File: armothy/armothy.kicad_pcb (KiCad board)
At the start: 2 copper layers, 90.2 x 59.7 mm, 21 parts, among them J1 I2C, J2 UART, J3 motZ, J4 pump, J5 valve, J6 Encoder, J7 Limit switch, J8 12V_PWR, J9 Conn_01x03_Female, U1 L293D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

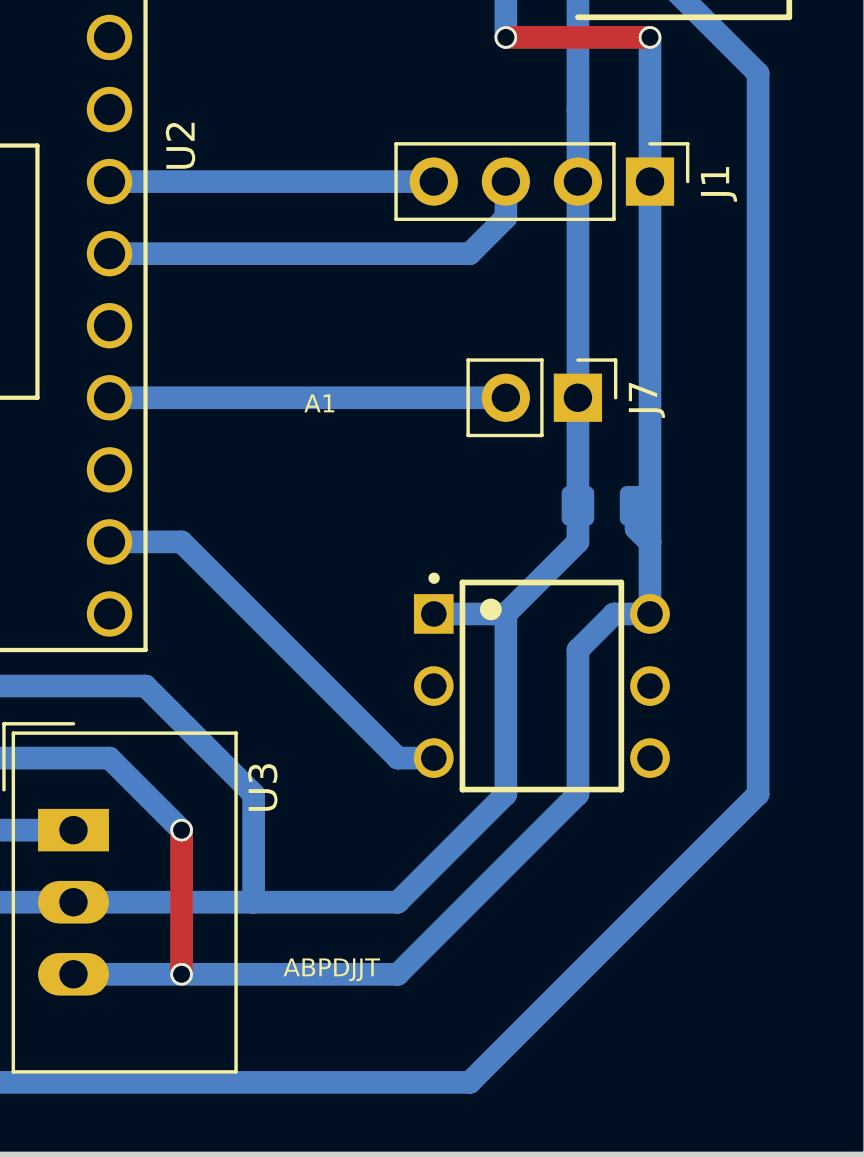
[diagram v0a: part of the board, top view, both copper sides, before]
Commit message: Adds 3D models, fix ABPDJJT footprint (fix #1).
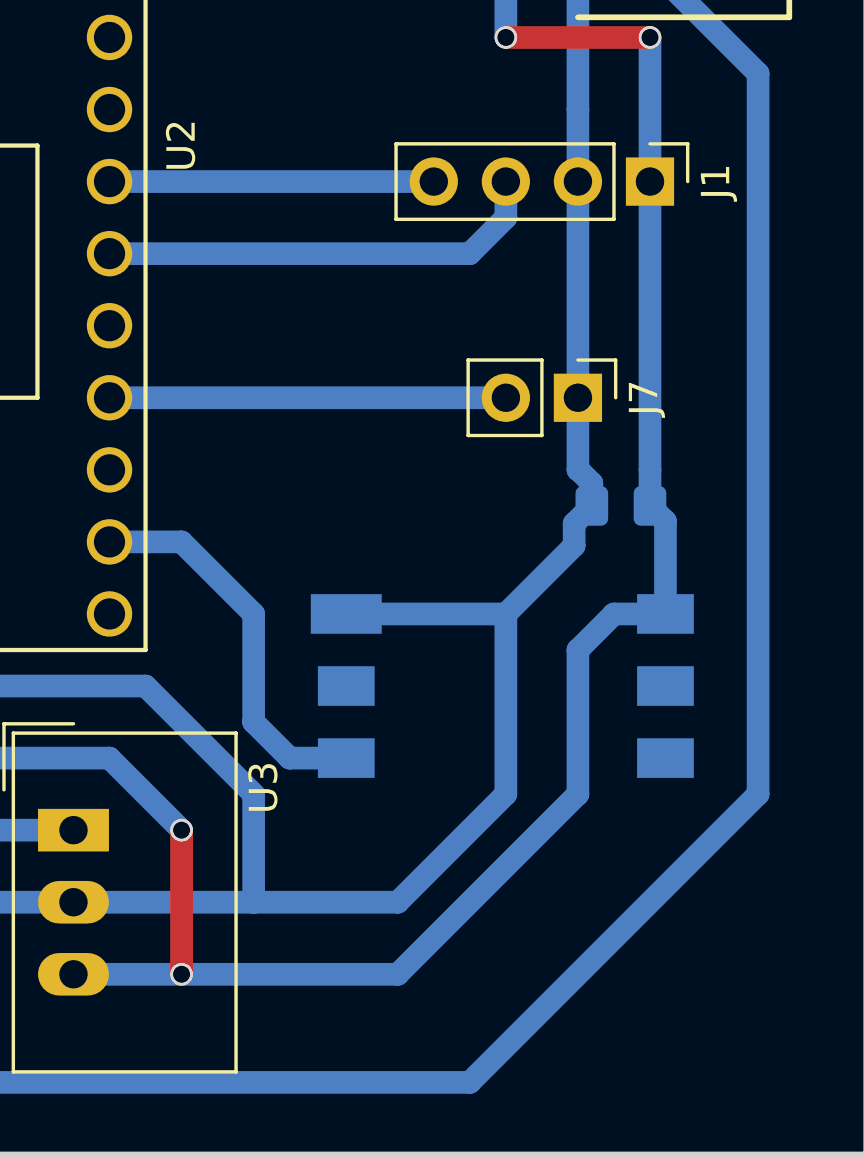
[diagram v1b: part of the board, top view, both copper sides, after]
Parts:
- A1: moved to B.Cu
- D1: footprint LED_SMD:LED_WS2812B_PLCC4_5.0x5.0mm_P3.2mm -> leds:LED_WS2812B_5.0x5.0mm
- moved A1 1.27 mm to (156.2, 101.6)
- moved C1 0.49 mm to (160.3, 95.2)
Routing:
- net GND: track 320.0 -> 323.5 mm
- net /PRESSURE: track 14.6 -> 13.7 mm
- net +5V: track 203.7 -> 203.0 mm

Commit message: Armothy controller V2.0
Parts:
- removed U1: L293D, Package_DIP:DIP-16_W7.62mm_LongPads
- added C6: 100n, Capacitor_SMD:C_0805_2012Metric_Pad1.15x1.40mm_HandSolder, B.Cu at (138.4, 103.9)
- added C7: 100n, Capacitor_SMD:C_0805_2012Metric_Pad1.15x1.40mm_HandSolder, B.Cu at (135.9, 103.9)
- added C8: 100n, Capacitor_SMD:C_0805_2012Metric_Pad1.15x1.40mm_HandSolder, B.Cu at (123.2, 100.3)
- added J10: I2C, Connector_PinHeader_2.54mm:PinHeader_1x04_P2.54mm_Vertical, F.Cu at (154.9, 77.5)
- added Q1: IRL6283M, mosfets:SOT-23, B.Cu at (122.1, 81.6)
- added Q2: IRL6283M, mosfets:SOT-23, B.Cu at (122.1, 86.0)
- added R3: 2.2K, Resistor_SMD:R_0805_2012Metric_Pad1.15x1.40mm_HandSolder, B.Cu at (138.0, 83.8)
- added R4: 2.2K, Resistor_SMD:R_0805_2012Metric_Pad1.15x1.40mm_HandSolder, B.Cu at (138.0, 86.4)
- added R5: 5K, Resistor_SMD:R_0805_2012Metric_Pad1.15x1.40mm_HandSolder, B.Cu at (130.8, 95.0)
- added R6: 10K, Resistor_SMD:R_0805_2012Metric_Pad1.15x1.40mm_HandSolder, B.Cu at (133.3, 95.0)
- added R7: 100, Resistor_SMD:R_0805_2012Metric_Pad1.15x1.40mm_HandSolder, B.Cu at (139.2, 99.3)
- added REF**: MountingHole_3.2mm_M3_Pad, MountingHole:MountingHole_3.2mm_M3_Pad, F.Cu at (157.0, 60.0)
- added REF**: MountingHole_3.2mm_M3_Pad, MountingHole:MountingHole_3.2mm_M3_Pad, F.Cu at (107.0, 120.0)
- added REF**: MountingHole_3.2mm_M3_Pad, MountingHole:MountingHole_3.2mm_M3_Pad, F.Cu at (107.0, 60.0)
- added REF**: MountingHole_3.2mm_M3_Pad, MountingHole:MountingHole_3.2mm_M3_Pad, F.Cu at (157.0, 120.0)
- added TP1: TestPoint, TestPoint:TestPoint_Pad_D1.0mm, B.Cu at (138.4, 71.1)
- added TP2: TestPoint, TestPoint:TestPoint_Pad_D1.0mm, B.Cu at (138.4, 73.7)
- added TP3: TestPoint, TestPoint:TestPoint_Pad_D1.0mm, B.Cu at (138.4, 78.7)
- added TP4: TestPoint, TestPoint:TestPoint_Pad_D1.0mm, B.Cu at (138.4, 76.2)
- added U5: ACS712xLCTR-05B, Package_SO:SOIC-8_3.9x4.9mm_P1.27mm, B.Cu at (129.5, 105.4)
- added U6: A4953_LJ, Package_SO:SOIC-8-1EP_3.9x4.9mm_P1.27mm_EP2.35x2.35mm, B.Cu at (119.4, 99.1)
- A1, C1: moved to F.Cu
- D1: value WS2812B -> LED; footprint leds:LED_WS2812B_5.0x5.0mm -> LED_SMD:LED_0805_2012Metric_Pad1.15x1.40mm_HandSolder
- moved C5 46.2 mm to (153.9, 88.3)
- moved J9 46.2 mm to (115.6, 91.4)
- moved R1 38.2 mm to (130.2, 88.5), turned to 90 degrees
- moved D1 31.0 mm to (135.9, 99.3), turned to 90 degrees
- moved J6 25.9 mm to (114.3, 73.7)
- moved J5 25.0 mm to (114.3, 81.3)
- moved J3 24.5 mm to (116.8, 108.0), turned to 270 degrees
- moved C3 18.1 mm to (118.1, 115.3), turned to 90 degrees
- moved C2 17.8 mm to (131.4, 116.8), turned to 90 degrees
- moved C1 17.1 mm to (145.4, 103.8), turned to 90 degrees
- moved J4 16.2 mm to (114.3, 86.4), turned to 90 degrees
- moved C4 13.3 mm to (121.3, 112.8), turned to 270 degrees
- moved J8 12.5 mm to (113.0, 114.3), turned to 0 degrees
- moved U4 10.9 mm to (124.5, 116.8), turned to 90 degrees
- moved U3 10.2 mm to (142.2, 116.8), turned to 90 degrees
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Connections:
- A1 pad 2: Net-(A1-Pad2) -> (no net)
- A1 pad 4: Net-(A1-Pad4) -> (no net)
- A1 pad 5: Net-(A1-Pad5) -> (no net)
- C2 pad 1: /POWER -> +12V
- C3 pad 1: /POWER -> +12V
- C5 pad 1: +5V -> /LIM_SWITCH
- D1 pad 1: +5V -> GND
- J4 pad 1: /POWER -> +12V
- J5 pad 1: Net-(J5-Pad1) -> +12V
- J5 pad 2: GND -> Net-(J5-Pad2)
- J8 pad 2: /POWER -> +12V
- U2 pad 12: /MOTORZ_PWM -> /MOTORZ_A
- U2 pad 13: /ENC_A -> (no net)
- U2 pad 14: /ENC_B -> (no net)
- U2 pad 20: Net-(U2-Pad20) -> /STATUS_LED
- U2 pad 22: Net-(U2-Pad22) -> /Z_CURRENT
- U2 pad 24: Net-(U2-Pad24) -> (no net)
- U2 pad 27: Net-(U2-Pad27) -> (no net)
- U2 pad 4: /MOTORZ_A -> /ENC_B
- U2 pad 5: Net-(U2-Pad5) -> /ENC_A
- U2 pad 6: /RGB_LED -> (no net)
- U3 pad 1: /POWER -> +12V
- U4 pad 1: /POWER -> +12V
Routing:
- net GND: track 323.5 -> 224.5 mm, vias 0 -> 5
- net +12V: track 0.00 -> 87.7 mm, vias 0 -> 2
- net /POWER: track 77.8 -> 0.00 mm, vias 2 -> 0
- net /RX_DYN: track 63.6 -> 6.18 mm, vias 2 -> 0
- net /VALVE_CTRL: track 60.1 -> 4.07 mm
- net /MOTORZ_PWM: track 45.3 -> 0.00 mm, vias 2 -> 0
- net /MOTORZ_A: track 52.8 -> 8.62 mm, vias 2 -> 0
- net +10V: track 77.0 -> 39.6 mm
- net /PUMP_CTRL: track 28.2 -> 4.34 mm
- net /MOTORZ_B: track 28.2 -> 10.9 mm
- net +5V: track 203.0 -> 189.0 mm, vias 8 -> 3
- net Net-(R5-Pad1): track 0.00 -> 12.0 mm
- net Net-(U5-Pad3): track 0.00 -> 11.7 mm
- net /Z_CURRENT: track 0.00 -> 11.4 mm
- net /RGB_LED: track 10.3 -> 0.00 mm
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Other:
- board size 90.2 x 59.7 mm -> 58 x 68 mm
- net class Default: via_dia 0.8 -> 1; via_drill 0.6 -> 0.8
- board text added: "Armothy v2"
- board text added: "Dyn"
- board text added: "ENC"
- board text added: "Fab@RustyDucks 2019"
- board text added: "I2C"
- board text added: "Limit"
- board text added: "Pump"
- board text added: "U1"
- board text added: "USB"
- board text added: "Valve"
- board text added: "Z"

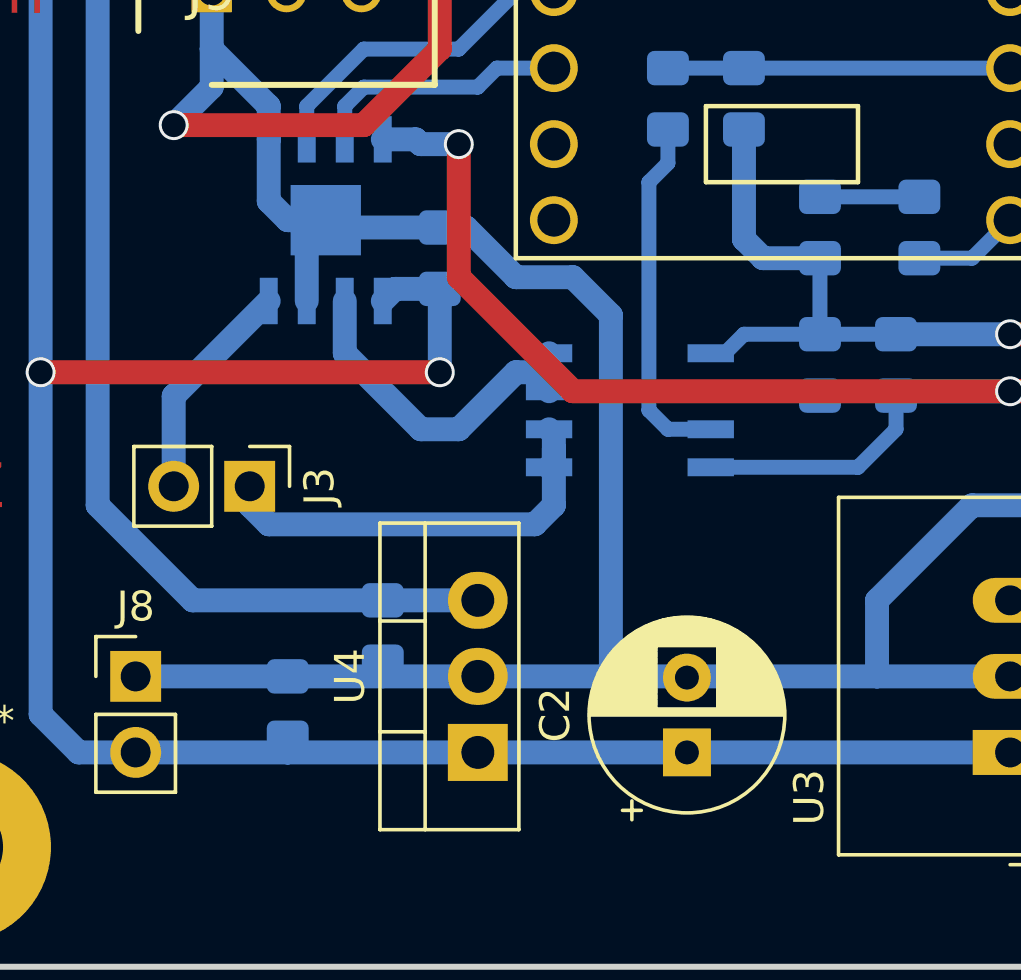
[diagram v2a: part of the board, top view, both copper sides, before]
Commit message: Changes LED footprint.
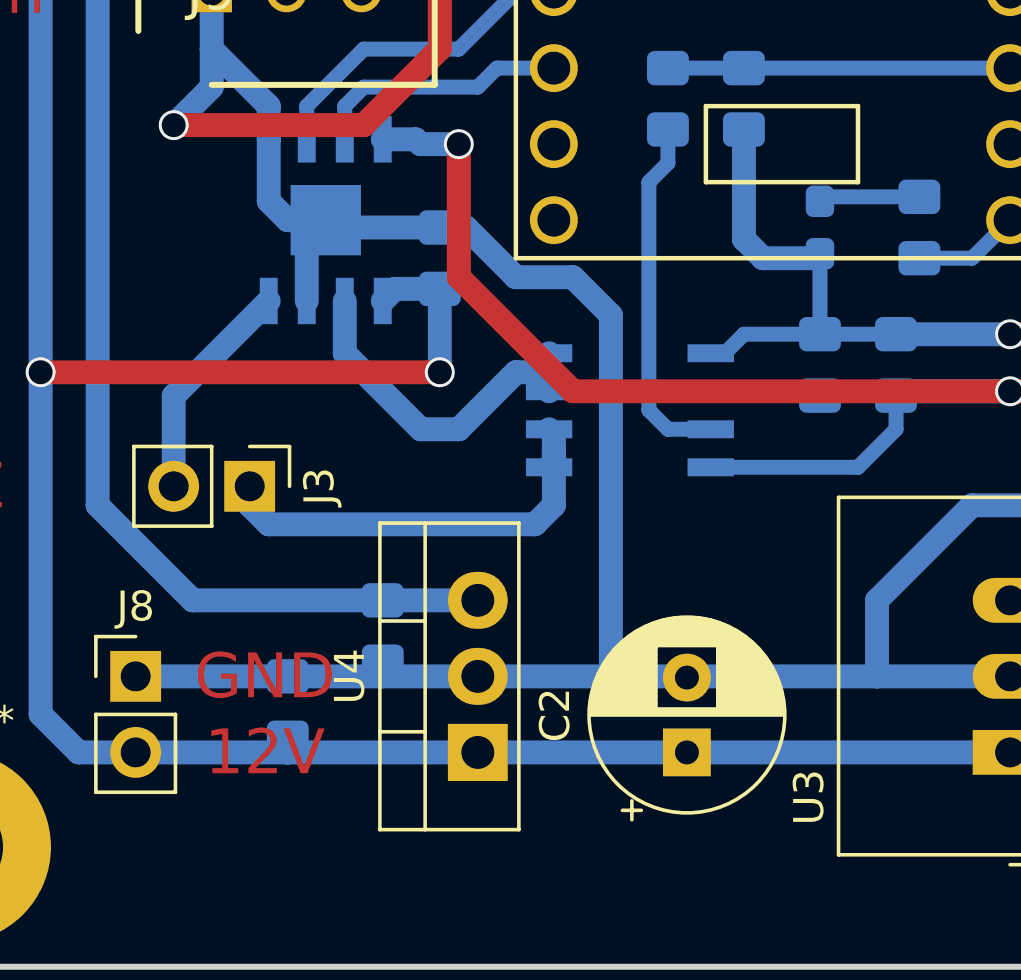
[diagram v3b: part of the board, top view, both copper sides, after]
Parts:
- D1: footprint LED_SMD:LED_0805_2012Metric_Pad1.15x1.40mm_HandSolder -> LED_SMD:LED_0603_1608Metric_Pad1.05x0.95mm_HandSolder
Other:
- board text added: "12V"
- board text added: "GND"
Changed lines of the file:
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@@
   (general
     (thickness 1.6)
-    (drawings 15)
+    (drawings 17)
     (tracks 231)
     (zones 0)
@@
   )
   (page A4)
+  (title_block
+    (title "Armothy controller")
+    (date 2019-02-18)
+    (rev 2.0)
+    (comment 1 Fabien-B)
+  )
   (layers
     (0 F.Cu signal)
@@
   )
   (setup
-    (last_trace_width 0.8)
+    (last_trace_width 0.508)
     (user_trace_width 0.3)
     (user_trace_width 0.5)
@@
     )
   )
-  (module LED_SMD:LED_0805_2012Metric_Pad1.15x1.40mm_HandSolder (layer B.Cu)
-    (at 135.89 99.305 90)
-    (descr "LED SMD 0805 (2012 Metric), square (rectangular) end terminal, IPC_7351 nominal, (Body size source: https://docs.google.com/spreadsheets/d/1BsfQQcO9C6DZCsRaXUlFlo91Tg2WpOkGARC1WS5S8t0/edit?usp=sharing), generated with kicad-footprint-generator")
-    (tags "LED handsolder")
-    (attr smd)
-    (fp_text reference D1 (at 0 1.65 90) (layer B.SilkS)
-      (effects (font (size 1 1) (thickness 0.15)) (justify mirror))
-    )
-    (fp_text value LED (at 0 -1.65 90) (layer B.Fab)
-      (effects (font (size 1 1) (thickness 0.15)) (justify mirror))
-    )
-    (fp_line (start 1 0.6) (end -0.7 0.6) (layer B.Fab) (width 0.1))
-    (fp_line (start -0.7 0.6) (end -1 0.3) (layer B.Fab) (width 0.1))
-    (fp_line (start -1 0.3) (end -1 -0.6) (layer B.Fab) (width 0.1))
-    (fp_line (start -1 -0.6) (end 1 -0.6) (layer B.Fab) (width 0.1))
-    (fp_line (start 1 -0.6) (end 1 0.6) (layer B.Fab) (width 0.1))
-    (fp_line (start 1 0.96) (end -1.86 0.96) (layer B.SilkS) (width 0.12))
-    (fp_line (start -1.86 0.96) (end -1.86 -0.96) (layer B.SilkS) (width 0.12))
-    (fp_line (start -1.86 -0.96) (end 1 -0.96) (layer B.SilkS) (width 0.12))
-    (fp_line (start -1.85 -0.95) (end -1.85 0.95) (layer B.CrtYd) (width 0.05))
-    (fp_line (start -1.85 0.95) (end 1.85 0.95) (layer B.CrtYd) (width 0.05))
-    (fp_line (start 1.85 0.95) (end 1.85 -0.95) (layer B.CrtYd) (width 0.05))
-    (fp_line (start 1.85 -0.95) (end -1.85 -0.95) (layer B.CrtYd) (width 0.05))
-    (fp_text user %R (at 0 0 90) (layer B.Fab)
-      (effects (font (size 0.5 0.5) (thickness 0.08)) (justify mirror))
-    )
-    (pad 1 smd roundrect (at -1.025 0 90) (size 1.15 1.4) (layers B.Cu B.Paste B.Mask) (roundrect_rratio 0.217391)
-      (net 1 GND))
-    (pad 2 smd roundrect (at 1.025 0 90) (size 1.15 1.4) (layers B.Cu B.Paste B.Mask) (roundrect_rratio 0.217391)
-      (net 15 "Net-(D1-Pad2)"))
-    (model ${KISYS3DMOD}/LED_SMD.3dshapes/LED_0805_2012Metric.wrl
-      (at (xyz 0 0 0))
-      (scale (xyz 1 1 1))
-      (rotate (xyz 0 0 0))
-    )
-  )
   (module Connector_PinHeader_2.54mm:PinHeader_1x04_P2.54mm_Vertical (layer F.Cu)
     (at 154.94 77.47 270)
@@
       (net 32 "Net-(TP4-Pad1)"))
   )
+  (module LED_SMD:LED_0603_1608Metric_Pad1.05x0.95mm_HandSolder (layer B.Cu)
+    (at 135.89 99.305 90)
+    (descr "LED SMD 0603 (1608 Metric), square (rectangular) end terminal, IPC_7351 nominal, (Body size source: http://www.tortai-tech.com/upload/download/2011102023233369053.pdf), generated with kicad-footprint-generator")
+    (tags "LED handsolder")
+    (attr smd)
+    (fp_text reference D1 (at 0 1.43 90) (layer B.SilkS)
+      (effects (font (size 1 1) (thickness 0.15)) (justify mirror))
+    )
+    (fp_text value LED (at 0 -1.43 90) (layer B.Fab)
+      (effects (font (size 1 1) (thickness 0.15)) (justify mirror))
+    )
+    (fp_line (start 0.8 0.4) (end -0.5 0.4) (layer B.Fab) (width 0.1))
+    (fp_line (start -0.5 0.4) (end -0.8 0.1) (layer B.Fab) (width 0.1))
+    (fp_line (start -0.8 0.1) (end -0.8 -0.4) (layer B.Fab) (width 0.1))
+    (fp_line (start -0.8 -0.4) (end 0.8 -0.4) (layer B.Fab) (width 0.1))
+    (fp_line (start 0.8 -0.4) (end 0.8 0.4) (layer B.Fab) (width 0.1))
+    (fp_line (start 0.8 0.735) (end -1.66 0.735) (layer B.SilkS) (width 0.12))
+    (fp_line (start -1.66 0.735) (end -1.66 -0.735) (layer B.SilkS) (width 0.12))
+    (fp_line (start -1.66 -0.735) (end 0.8 -0.735) (layer B.SilkS) (width 0.12))
+    (fp_line (start -1.65 -0.73) (end -1.65 0.73) (layer B.CrtYd) (width 0.05))
+    (fp_line (start -1.65 0.73) (end 1.65 0.73) (layer B.CrtYd) (width 0.05))
+    (fp_line (start 1.65 0.73) (end 1.65 -0.73) (layer B.CrtYd) (width 0.05))
+    (fp_line (start 1.65 -0.73) (end -1.65 -0.73) (layer B.CrtYd) (width 0.05))
+    (fp_text user %R (at 0 0 90) (layer B.Fab)
+      (effects (font (size 0.4 0.4) (thickness 0.06)) (justify mirror))
+    )
+    (pad 1 smd roundrect (at -0.875 0 90) (size 1.05 0.95) (layers B.Cu B.Paste B.Mask) (roundrect_rratio 0.25)
+      (net 1 GND))
+    (pad 2 smd roundrect (at 0.875 0 90) (size 1.05 0.95) (layers B.Cu B.Paste B.Mask) (roundrect_rratio 0.25)
+      (net 15 "Net-(D1-Pad2)"))
+    (model ${KISYS3DMOD}/LED_SMD.3dshapes/LED_0603_1608Metric.wrl
+      (at (xyz 0 0 0))
+      (scale (xyz 1 1 1))
+      (rotate (xyz 0 0 0))
+    )
+  )
+  (gr_text 12V (at 117.348 116.84) (layer F.Cu)
+    (effects (font (size 1.5 1.5) (thickness 0.3)))
+  )
+  (gr_text GND (at 117.348 114.3) (layer F.Cu)
+    (effects (font (size 1.5 1.5) (thickness 0.3)))
+  )
   (gr_text "Fab@RustyDucks 2019" (at 133.35 59.69) (layer B.Cu)

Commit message: latest changes
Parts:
- removed the REF** at (157.0, 60.0)
- removed the REF** at (107.0, 120.0)
- removed the REF** at (107.0, 60.0)
- removed the REF** at (157.0, 120.0)
- removed TP2: TestPoint, TestPoint:TestPoint_Pad_D1.0mm
- removed U6: A4953_LJ, Package_SO:SOIC-8-1EP_3.9x4.9mm_P1.27mm_EP2.35x2.35mm
- added IC1: TLE52052GAUMA1, TLE5205:TLE52052GAUMA1, B.Cu at (115.3, 92.7)
- added REF**: MountingHole_3.2mm_M3_DIN965_Pad, MountingHole:MountingHole_3.2mm_M3_DIN965_Pad, F.Cu at (157.0, 60.0)
- added REF**: MountingHole_3.2mm_M3_DIN965_Pad, MountingHole:MountingHole_3.2mm_M3_DIN965_Pad, F.Cu at (157.0, 116.0)
- added REF**: MountingHole_3.2mm_M3_DIN965_Pad, MountingHole:MountingHole_3.2mm_M3_DIN965_Pad, F.Cu at (107.0, 116.0)
- added REF**: MountingHole_3.2mm_M3_DIN965_Pad, MountingHole:MountingHole_3.2mm_M3_DIN965_Pad, F.Cu at (107.0, 60.0)
- added REF**: USB_LOGO, teensy:USB_LOGO, F.Cu at (134.6, 68.6)
- C1: moved to B.Cu
- C2: value 10u -> 100u
- moved C1 36.9 mm to (138.2, 67.6), turned to 270 degrees
- moved A1 35.6 mm to (149.9, 68.6)
- moved C4 33.8 mm to (154.4, 106.2), turned to 180 degrees
- moved J9 33.7 mm to (141.2, 113.3), turned to 270 degrees
- moved C3 33.5 mm to (150.4, 106.2), turned to 0 degrees
- moved U4 26.1 mm to (149.9, 110.7), turned to 0 degrees
- moved C8 20.6 mm to (110.2, 84.3), turned to 180 degrees
- moved U3 17.0 mm to (149.9, 101.6), turned to 0 degrees
- moved D1 13.5 mm to (148.7, 95.0), turned to 180 degrees
- moved J8 12.0 mm to (125.0, 113.3), turned to 180 degrees
- moved R7 7.70 mm to (146.8, 98.1)
- moved R5 6.86 mm to (137.7, 95.0)
- moved R6 6.35 mm to (139.7, 95.0)
- moved C2 6.32 mm to (133.1, 110.7), turned to 270 degrees
- moved J3 4.88 mm to (119.9, 104.1)
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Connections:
- C8 pad 1: GND -> +12V
- C8 pad 2: +12V -> GND
- U2 pad 14: (no net) -> /MOTORZ_EF
- U2 pad 21: /PRESSURE -> (no net)
- U2 pad 30: Net-(TP2-Pad1) -> /PRESSURE
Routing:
- net GND: track 224.5 -> 270.0 mm, vias 5 -> 7
- net +5V: track 189.0 -> 151.3 mm, vias 3 -> 1
- net +12V: track 87.7 -> 118.4 mm, vias 2 -> 0
- net /MOTORZ_EF: track 0.00 -> 17.3 mm
- net Net-(J9-Pad3): track 10.4 -> 23.3 mm, vias 0 -> 2
- net +10V: track 39.6 -> 26.8 mm, vias 0 -> 2
- net Net-(IC1-Pad1): track 7.51 -> 18.2 mm
- net Net-(J3-Pad1): track 14.6 -> 6.68 mm
- net /Z_CURRENT: track 11.4 -> 4.57 mm
- net Net-(R5-Pad1): track 12.0 -> 17.8 mm
- net /MOTORZ_B: track 10.9 -> 6.36 mm
- net Net-(TP2-Pad1): track 3.81 -> 0.00 mm
- net /MOTORZ_A: track 8.62 -> 6.36 mm
- net /LIM_SWITCH: track 13.5 -> 11.6 mm
- net /SDA: track 18.6 -> 17.5 mm
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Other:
- board size 58 x 68 mm -> 58 x 64 mm
- board text added: "Armothy V3"
- board text removed: "Armothy v2"
- board text removed: "GND"
- board text removed: "USB"
